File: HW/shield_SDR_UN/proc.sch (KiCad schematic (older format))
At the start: 40 parts

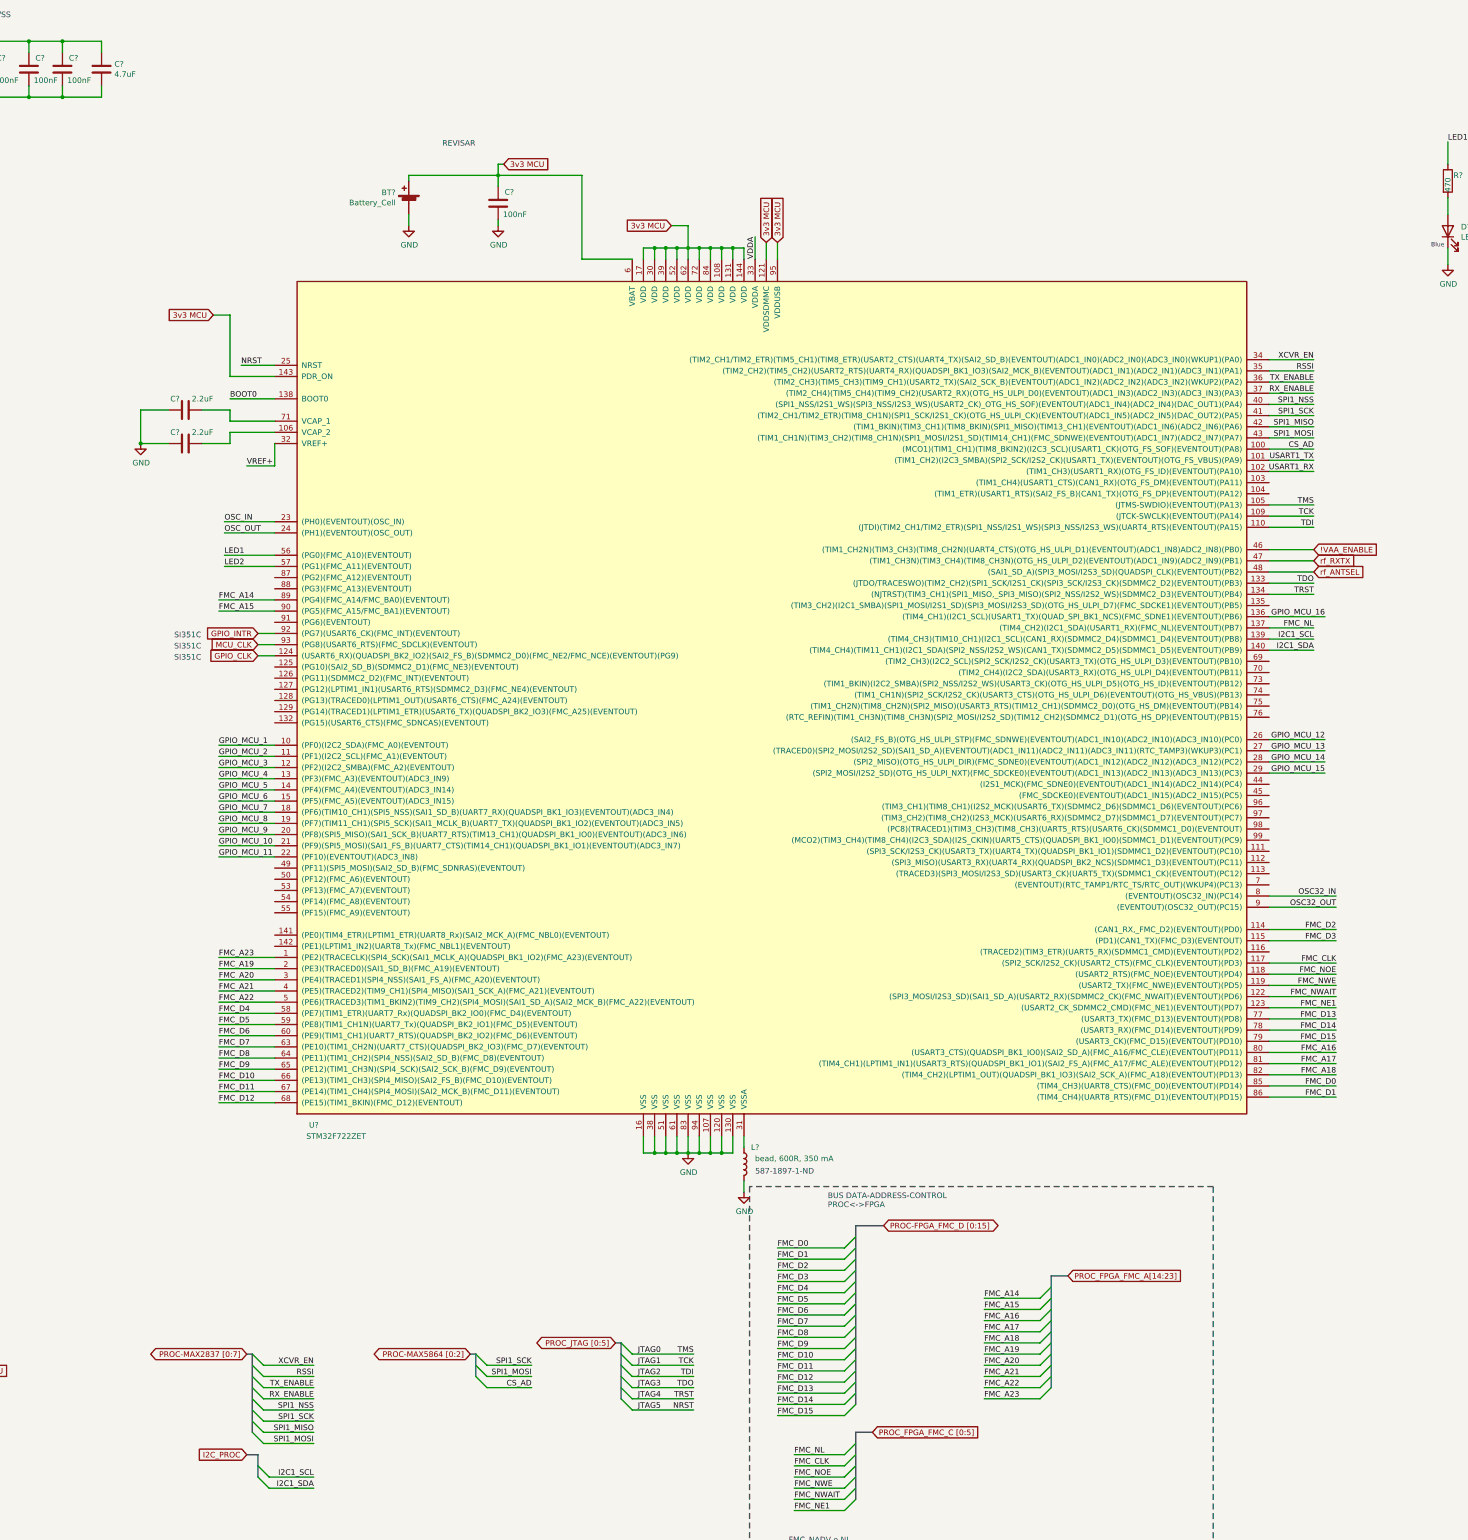
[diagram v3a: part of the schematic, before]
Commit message: JTAG routed
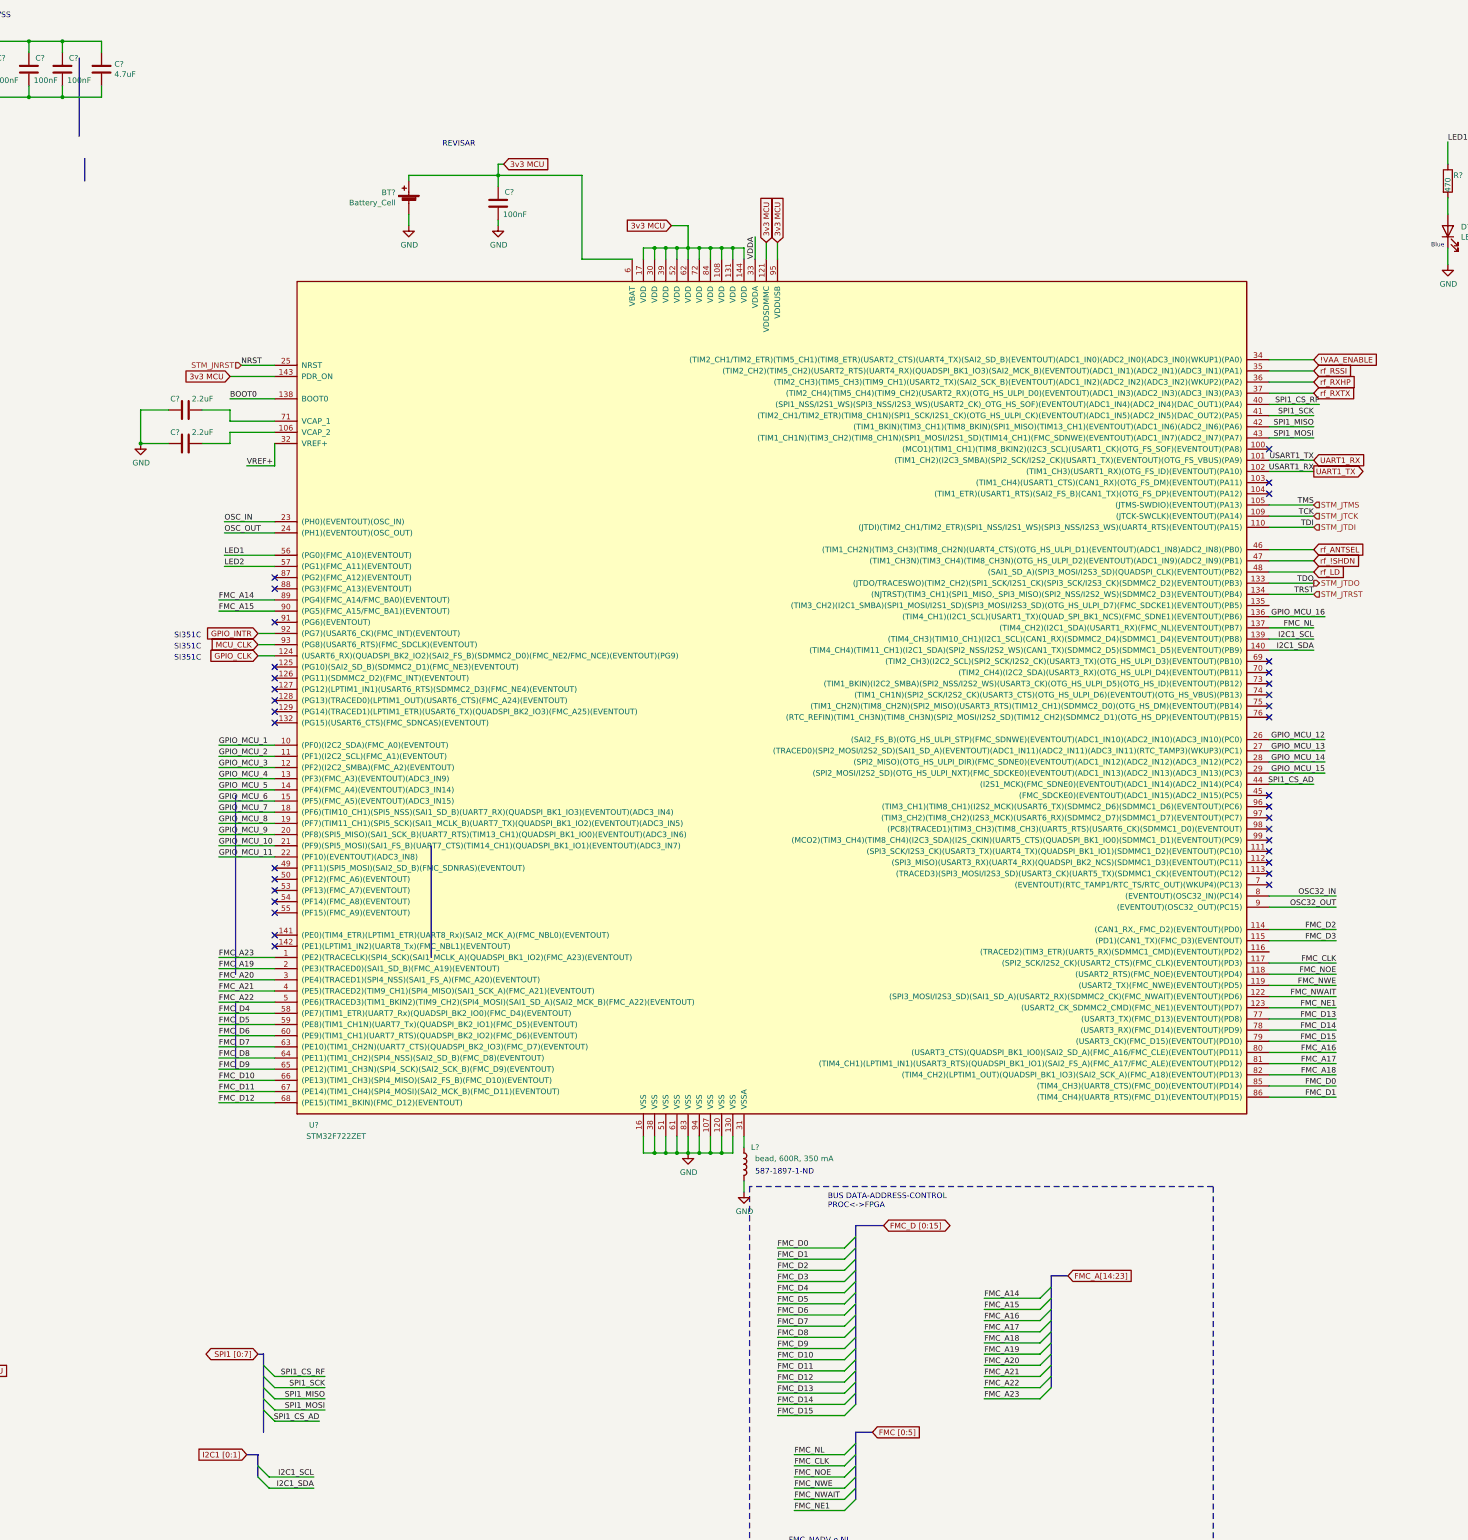
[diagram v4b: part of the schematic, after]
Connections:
- net RX_ENABLE is gone; now on net rf_RXTX: U?.37 ((TIM2_CH4)(TIM5_CH4)(TIM9_CH2)(USART2_RX)(OTG_HS_ULPI_D0)(EVENTOUT)(ADC1_IN3)(ADC2_IN3)(ADC3_IN3)(PA3))
- net XCVR_EN is gone; now on net !VAA_ENABLE: U?.34 ((TIM2_CH1/TIM2_ETR)(TIM5_CH1)(TIM8_ETR)(USART2_CTS)(UART4_TX)(SAI2_SD_B)(EVENTOUT)(ADC1_IN0)(ADC2_IN0)(ADC3_IN0)(WKUP1)(PA0))
- net !VAA_ENABLE: no longer U?.46 ((TIM1_CH2N)(TIM3_CH3)(TIM8_CH2N)(UART4_CTS)(OTG_HS_ULPI_D1)(EVENTOUT)(ADC1_IN8)ADC2_IN8)(PB0))
- net rf_ANTSEL: now also U?.46 ((TIM1_CH2N)(TIM3_CH3)(TIM8_CH2N)(UART4_CTS)(OTG_HS_ULPI_D1)(EVENTOUT)(ADC1_IN8)ADC2_IN8)(PB0)); no longer U?.48 ((SAI1_SD_A)(SPI3_MOSI/I2S3_SD)(QUADSPI_CLK)(EVENTOUT)(PB2))
- net rf_RXTX: no longer U?.47 ((TIM1_CH3N)(TIM3_CH4)(TIM8_CH3N)(OTG_HS_ULPI_D2)(EVENTOUT)(ADC1_IN9)(ADC2_IN9)(PB1))
- net SPI1_CS_AD: now reaches U?.44 ((I2S1_MCK)(FMC_SDNE0)(EVENTOUT)(ADC1_IN14)(ADC2_IN14)(PC4))
- net CS_AD: no longer names the net of U?.100 ((MCO1)(TIM1_CH1)(TIM8_BKIN2)(I2C3_SCL)(USART1_CK)(OTG_FS_SOF)(EVENTOUT)(PA8))
- net JTAG0 renamed STM_JTMS
- net JTAG1 renamed STM_JTCK
- net JTAG2 renamed STM_JTDI
- net JTAG3 renamed STM_JTDO
- net JTAG4 renamed STM_JTRST
- net JTAG5 renamed STM_JNRST
- net RSSI renamed rf_RSSI
- net SPI1_NSS renamed SPI1_CS_RF
- net TX_ENABLE renamed rf_RXHP
- net USART1_RX renamed UART1_TX
- net USART1_TX renamed UART1_RX
- new net rf_!SHDN: U?.47 ((TIM1_CH3N)(TIM3_CH4)(TIM8_CH3N)(OTG_HS_ULPI_D2)(EVENTOUT)(ADC1_IN9)(ADC2_IN9)(PB1))
- new net rf_LD: U?.48 ((SAI1_SD_A)(SPI3_MOSI/I2S3_SD)(QUADSPI_CLK)(EVENTOUT)(PB2))
- no-connect marks 0 -> 34
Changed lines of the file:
@@
 Connection ~ 2400 1950
 Connection ~ 1400 950
-Text GLabel 5500 3400 0    50   Input ~ 0
+Text GLabel 5650 3950 0    50   Input ~ 0
 3v3 MCU
 Wire Wire Line
 	6050 3950 5650 3950
-Wire Wire Line
-	5650 3950 5650 3400
-Wire Wire Line
-	5650 3400 5500 3400
 Wire Wire Line
 	6050 4150 5650 4150
@@
 Wire Wire Line
 	14950 4800 15350 4800
-Text Label 15350 4700 2    50   ~ 0
-USART1_TX
-Text Label 15350 4800 2    50   ~ 0
-USART1_RX
-Wire Wire Line
-	14950 4200 15350 4200
-Text Label 15350 4200 2    50   ~ 0
-SPI1_NSS
 Text Label 15350 4300 2    50   ~ 0
 SPI1_SCK
@@
 Wire Wire Line
 	14950 3900 15350 3900
-Text Label 15350 3900 2    50   ~ 0
-RSSI
-Wire Wire Line
-	14950 3800 15350 3800
-Wire Wire Line
-	14950 4000 15350 4000
-Wire Wire Line
-	14950 4100 15350 4100
-Text Label 15350 4100 2    50   ~ 0
-RX_ENABLE
-Text Label 15350 4000 2    50   ~ 0
-TX_ENABLE
-Entry Wire Line
-	5850 12700 5950 12800
-Entry Wire Line
-	5850 12800 5950 12900
-Entry Wire Line
-	5850 12900 5950 13000
-Entry Wire Line
-	5850 13000 5950 13100
-Entry Wire Line
-	5850 13100 5950 13200
-Entry Wire Line
-	5850 13200 5950 13300
-Entry Wire Line
-	5850 13300 5950 13400
-Entry Wire Line
-	5850 13400 5950 13500
-Text Label 15350 3800 2    50   ~ 0
-XCVR_EN
-Text Label 6400 12800 2    50   ~ 0
-XCVR_EN
-Text Label 6400 12900 2    50   ~ 0
-RSSI
-Text Label 6400 13000 2    50   ~ 0
-TX_ENABLE
-Text Label 6400 13100 2    50   ~ 0
-RX_ENABLE
-Text Label 6400 13200 2    50   ~ 0
-SPI1_NSS
-Text Label 6400 13300 2    50   ~ 0
-SPI1_SCK
-Text Label 6400 13400 2    50   ~ 0
-SPI1_MISO
-Text Label 6400 13500 2    50   ~ 0
-SPI1_MOSI
-Wire Wire Line
-	6400 12800 5950 12800
-Wire Wire Line
-	6400 12900 5950 12900
-Wire Wire Line
-	6400 13000 5950 13000
-Wire Wire Line
-	6400 13100 5950 13100
-Wire Wire Line
-	6400 13200 5950 13200
-Wire Wire Line
-	6400 13300 5950 13300
-Wire Wire Line
-	6400 13400 5950 13400
-Wire Wire Line
-	6400 13500 5950 13500
-Text GLabel 5800 12700 0    50   BiDi ~ 0
-PROC-MAX2837 [0:7]
-Wire Bus Line
-	5850 12700 5800 12700
-Wire Wire Line
-	14950 4600 15350 4600
-Text Label 15350 4600 2    50   ~ 0
-CS_AD
-Text Label 8350 12800 2    50   ~ 0
-SPI1_SCK
-Text Label 8350 12900 2    50   ~ 0
-SPI1_MOSI
-Wire Wire Line
-	8350 12800 7950 12800
-Wire Wire Line
-	7950 13000 8350 13000
-Text Label 8350 13000 2    50   ~ 0
-CS_AD
-Wire Wire Line
-	7950 12900 8350 12900
-Entry Wire Line
-	7850 12700 7950 12800
-Entry Wire Line
-	7850 12800 7950 12900
-Entry Wire Line
-	7850 12900 7950 13000
-Wire Bus Line
-	7850 12700 7800 12700
-Text GLabel 7800 12700 0    50   BiDi ~ 0
-PROC-MAX5864 [0:2]
+Wire Wire Line
+	14950 7600 15350 7600
+Text Label 15350 7600 2    50   ~ 0
+SPI1_CS_AD
 Wire Wire Line
 	15350 5100 14950 5100
 Wire Wire Line
 	15350 5200 14950 5200
-Text Label 9800 12700 2    50   ~ 0
-TMS
-Text Label 9800 12800 2    50   ~ 0
-TCK
-Text Label 9800 13000 2    50   ~ 0
-TDO
-Text Label 9800 12900 2    50   ~ 0
-TDI
-Text Label 9800 13100 2    50   ~ 0
-TRST
-Entry Wire Line
-	9150 12600 9250 12700
-Entry Wire Line
-	9150 12700 9250 12800
-Entry Wire Line
-	9150 12800 9250 12900
-Entry Wire Line
-	9150 12900 9250 13000
-Entry Wire Line
-	9150 13000 9250 13100
-Wire Bus Line
-	9150 12600 9100 12600
-Text GLabel 9100 12600 0    50   BiDi ~ 0
-PROC_JTAG [0:5]
-Entry Wire Line
-	9150 13100 9250 13200
-Text Label 9800 13200 2    50   ~ 0
-NRST
-Wire Wire Line
-	9250 12700 9800 12700
-Wire Wire Line
-	9250 12800 9800 12800
-Wire Wire Line
-	9250 12900 9800 12900
-Wire Wire Line
-	9250 13000 9800 13000
-Wire Wire Line
-	9250 13100 9800 13100
-Wire Wire Line
-	9250 13200 9800 13200
-Text Label 9300 12800 0    50   ~ 0
-JTAG1
-Text Label 9300 12700 0    50   ~ 0
-JTAG0
-Text Label 9300 12900 0    50   ~ 0
-JTAG2
-Text Label 9300 13000 0    50   ~ 0
-JTAG3
-Text Label 9300 13100 0    50   ~ 0
-JTAG4
-Text Label 9300 13200 0    50   ~ 0
-JTAG5
 Wire Wire Line
 	14950 5500 15350 5500
-Text GLabel 15350 5500 2    50   Input ~ 0
-!VAA_ENABLE
 Wire Wire Line
 	14950 8900 15550 8900
@@
 	11250 12450 11150 12550
 Text GLabel 11500 11550 2    50   BiDi ~ 0
-PROC-FPGA_FMC_D [0:15]
+FMC_D [0:15]
 Wire Wire Line
 	1500 9800 1850 9800
@@
 	11250 13400 11400 13400
 Text GLabel 11400 13400 2    50   Input ~ 0
-PROC_FPGA_FMC_C [0:5]
+FMC [0:5]
 Wire Wire Line
 	14950 10000 15550 10000
@@
 	13000 12000 13150 12000
 Text GLabel 13150 12000 2    50   Input ~ 0
-PROC_FPGA_FMC_A[14:23]
+FMC_A[14:23]
 Entry Wire Line
 	12900 12200 13000 12100
@@
 	5900 13600 5800 13600
 Text GLabel 5800 13600 0    50   Input ~ 0
-I2C_PROC
+I2C1 [0:1]
 Text Label 5550 7950 0    50   ~ 0
 GPIO_MCU_8
@@
 Wire Wire Line
 	6050 6450 5900 6450
+Wire Wire Line
+	15350 5600 14950 5600
+Wire Wire Line
+	14950 5700 15350 5700
+Text GLabel 15350 4800 2    50   Output ~ 0
+UART1_TX
+Text GLabel 15350 4700 2    50   Input ~ 0
+UART1_RX
+Text GLabel 15350 3900 2    50   Input ~ 0
+rf_RSSI
+Entry Wire Line
+	5950 12900 6050 13000
+Entry Wire Line
+	5950 13000 6050 13100
+Entry Wire Line
+	5950 13100 6050 13200
+Text Label 6500 13000 2    50   ~ 0
+SPI1_SCK
+Text Label 6500 13100 2    50   ~ 0
+SPI1_MISO
+Text Label 6500 13200 2    50   ~ 0
+SPI1_MOSI
+Wire Wire Line
+	6500 12900 6050 12900
+Wire Wire Line
+	6500 13000 6050 13000
+Wire Wire Line
+	6500 13100 6050 13100
+Wire Wire Line
+	6500 13200 6050 13200
+Text GLabel 5900 12700 0    50   BiDi ~ 0
+SPI1 [0:7]
+Wire Bus Line
+	5950 12700 5900 12700
+Wire Wire Line
+	6050 13300 6450 13300
+Text Label 6450 13300 2    50   ~ 0
+SPI1_CS_AD
+Entry Wire Line
+	5950 13200 6050 13300
+Text Label 6500 12900 2    50   ~ 0
+SPI1_CS_RF
+Entry Wire Line
+	5950 12800 6050 12900
+Wire Wire Line
+	15400 4200 14950 4200
+Text Label 15400 4200 2    50   ~ 0
+SPI1_CS_RF
+Text GLabel 15350 5500 2    50   Input ~ 0
+rf_ANTSEL
+Text GLabel 15350 4100 2    50   Input ~ 0
+rf_RXTX
+Text GLabel 15350 4000 2    50   Input ~ 0
+rf_RXHP
 Text GLabel 15350 5600 2    50   Input ~ 0
-rf_RXTX
+rf_!SHDN
 Text GLabel 15350 5700 2    50   Input ~ 0
-rf_ANTSEL
-Wire Wire Line
-	15350 5600 14950 5600
-Wire Wire Line
-	14950 5700 15350 5700
+rf_LD
+Text GLabel 15350 3800 2    50   Input ~ 0
+!VAA_ENABLE
+Wire Wire Line
+	15350 3800 14950 3800
+Wire Wire Line
+	15350 4000 14950 4000
+Wire Wire Line
+	15350 4100 14950 4100
+Text Label 15350 4800 2    50   ~ 0
+USART1_RX
+Text Label 15350 4700 2    50   ~ 0
+USART1_TX
+NoConn ~ 14950 8400
+NoConn ~ 14950 8300
+NoConn ~ 14950 8200
+NoConn ~ 14950 8100
+NoConn ~ 14950 8000
+NoConn ~ 14950 7900
+NoConn ~ 14950 7800
+NoConn ~ 14950 7700
+NoConn ~ 14950 7000
+NoConn ~ 14950 6900
+NoConn ~ 14950 6800
+NoConn ~ 14950 6700
+NoConn ~ 14950 6600
+NoConn ~ 14950 6500
+NoConn ~ 14950 5000
+NoConn ~ 14950 4900
+NoConn ~ 14950 4600
+NoConn ~ 6050 5750
+NoConn ~ 6050 5850
+NoConn ~ 6050 6150
+NoConn ~ 6050 6550
+NoConn ~ 6050 6650
+NoConn ~ 6050 6750
+NoConn ~ 6050 6850
+NoConn ~ 6050 6950
+NoConn ~ 6050 7050
+NoConn ~ 6050 8350
+NoConn ~ 6050 8450
+NoConn ~ 6050 8550
+NoConn ~ 6050 8650
+NoConn ~ 6050 8750
+NoConn ~ 6050 8950
+NoConn ~ 6050 9050
+NoConn ~ 14950 8500
 Wire Bus Line
-	7850 12700 7850 12900
+	7450 8150 7450 9150
+Wire Bus Line
+	5700 9550 5700 10150
+Wire Bus Line
+	5700 7700 5700 9300
+Wire Bus Line
+	4350 2000 4350 2200
+Wire Bus Line
+	4300 1100 4300 1800
+Text HLabel 15350 5800 2    50   Output ~ 0
+STM_JTDO
+Text HLabel 15350 5900 2    50   Input ~ 0
+STM_JTRST
+Text HLabel 15350 5300 2    50   Input ~ 0
+STM_JTDI
+Text HLabel 15350 5200 2    50   Input ~ 0
+STM_JTCK
+Text HLabel 15350 5100 2    50   Input ~ 0
+STM_JTMS
+Text HLabel 5750 3850 0    50   Input ~ 0
+STM_JNRST
 Wire Bus Line
 	5900 13600 5900 13800
 Wire Bus Line
-	9150 12600 9150 13100
-Wire Bus Line
-	5850 12700 5850 13400
-Wire Bus Line
 	11250 13400 11250 14000
 Wire Bus Line
+	5950 12700 5950 13400
+Wire Bus Line
 	13000 12000 13000 13000

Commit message: i2c_complete
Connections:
- net I2C1_SCL renamed I2C_SCL
- net I2C1_SDA renamed I2C_SDA
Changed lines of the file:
@@
 Wire Wire Line
 	15350 6200 14950 6200
-Text Label 6400 13800 2    50   ~ 0
-I2C1_SCL
-Wire Wire Line
-	6000 13800 6400 13800
-Text Label 6400 13900 2    50   ~ 0
-I2C1_SDA
-Wire Wire Line
-	6000 13900 6400 13900
-Entry Wire Line
-	5900 13700 6000 13800
-Entry Wire Line
-	5900 13800 6000 13900
-Wire Bus Line
-	5900 13600 5800 13600
-Text GLabel 5800 13600 0    50   Input ~ 0
-I2C1 [0:1]
 Text Label 5550 7950 0    50   ~ 0
 GPIO_MCU_8
@@
 NoConn ~ 14950 8500
 Wire Bus Line
-	7450 8150 7450 9150
-Wire Bus Line
-	5700 9550 5700 10150
-Wire Bus Line
-	5700 7700 5700 9300
-Wire Bus Line
 	4350 2000 4350 2200
 Wire Bus Line
@@
 Text HLabel 5750 3850 0    50   Input ~ 0
 STM_JNRST
-Wire Bus Line
-	5900 13600 5900 13800
+Text GLabel 15350 6300 2    50   Input ~ 0
+I2C_SCL
+Text GLabel 15350 6400 2    50   Input ~ 0
+I2C_SDA
 Wire Bus Line
 	11250 13400 11250 14000

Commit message: Schematic finished
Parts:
- removed C?: 100nF, Capacitor_SMD:C_0603_1608Metric_Pad1.05x0.95mm_HandSolder, symbol Device:C
- removed R?: 10k, Resistor_SMD:R_0603_1608Metric_Pad1.05x0.95mm_HandSolder, symbol Device:R
- removed SW?: SW_Push, SWITCH_FSM1LPA, symbol FSM1LPTR:FSM1LPTR
- added C99: 100nF, Capacitor_SMD:C_0603_1608Metric_Pad1.05x0.95mm_HandSolder, symbol Device:C
- added R54: 10k, Resistor_SMD:R_0603_1608Metric_Pad1.05x0.95mm_HandSolder, symbol Device:R
- added S4: TL1014BF160QG, lib:TL1014BF160QG, symbol TL1014BF160QG:TL1014BF160QG
- BT1: renamed from BT?; footprint modules:BAT-HLD-001 -> lib:MPD_BK-870; digikey BAT-HLD-001-ND -> BK-870-ND
- J3: renamed from J?; footprint Connector_PinHeader_2.54mm:PinHeader_2x20_P2.54mm_Vertical -> Connector_PinHeader_2.54mm:PinHeader_2x10_P2.54mm_Vertical
- gave numbers to parts that had none: 35
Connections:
- net 3V3 MCU: now also J3.1 (Pin_1), J3.11 (Pin_11); no longer J3.19 (Pin_19), J3.9 (Pin_9)
- net 3v3 MCU: now also R54.1
- net GND: now also C99.2, S4.3, S4.4
- net GPIO_CLK: now also U5.53 ((PF13)(FMC_A7)(EVENTOUT)); no longer U5.124 ((USART6_RX)(QUADSPI_BK2_IO2)(SAI2_FS_B)(SDMMC2_D0)(FMC_NE2/FMC_NCE)(EVENTOUT)(PG9))
- net GPIO_INTR: now also U5.49 ((PF11)(SPI5_MOSI)(SAI2_SD_B)(FMC_SDNRAS)(EVENTOUT)); no longer U5.92 ((PG7)(USART6_CK)(FMC_INT)(EVENTOUT))
- net GPIO_MCU_1: now also J3.2 (Pin_2); no longer J3.1 (Pin_1)
- net GPIO_MCU_10: now also J3.13 (Pin_13); no longer J3.12 (Pin_12)
- net GPIO_MCU_11: now also J3.14 (Pin_14); no longer J3.13 (Pin_13)
- net GPIO_MCU_12: now also J3.15 (Pin_15); no longer J3.14 (Pin_14)
- net GPIO_MCU_13: now also J3.16 (Pin_16); no longer J3.15 (Pin_15)
- net GPIO_MCU_14: now also J3.17 (Pin_17); no longer J3.16 (Pin_16)
- net GPIO_MCU_15: now also J3.18 (Pin_18); no longer J3.17 (Pin_17)
- net GPIO_MCU_16: now also J3.19 (Pin_19); no longer J3.18 (Pin_18)
- net GPIO_MCU_2: now also J3.3 (Pin_3); no longer J3.2 (Pin_2)
- net GPIO_MCU_3: now also J3.4 (Pin_4); no longer J3.3 (Pin_3)
- net GPIO_MCU_4: now also J3.5 (Pin_5); no longer J3.4 (Pin_4)
- net GPIO_MCU_5: now also J3.6 (Pin_6); no longer J3.5 (Pin_5)
- net GPIO_MCU_6: now also J3.7 (Pin_7); no longer J3.6 (Pin_6)
- net GPIO_MCU_7: now also J3.8 (Pin_8); no longer J3.7 (Pin_7)
- net GPIO_MCU_8: now also J3.9 (Pin_9); no longer J3.8 (Pin_8)
- net GPIO_MCU_9: now also J3.12 (Pin_12); no longer J3.11 (Pin_11)
- net MCU_CLK: now also U5.50 ((PF12)(FMC_A6)(EVENTOUT)); no longer U5.93 ((PG8)(USART6_RTS)(FMC_SDCLK)(EVENTOUT))
- net STM_JNRST: now also C99.1, R54.2, S4.1, S4.2
- net FMC_NBL0: now reaches U5.141 ((PE0)(TIM4_ETR)(LPTIM1_ETR)(UART8_Rx)(SAI2_MCK_A)(FMC_NBL0)(EVENTOUT))
- net FMC_NBL1: now reaches U5.142 ((PE1)(LPTIM1_IN2)(UART8_Tx)(FMC_NBL1)(EVENTOUT))
- no-connect marks 34 -> 33
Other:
- note added: "RTC Battery"
- note removed: "REVISAR\n"
- moved on the sheet: J3
